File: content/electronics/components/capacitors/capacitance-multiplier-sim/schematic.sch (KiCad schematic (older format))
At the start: 7 parts, among them Q1 2N2222

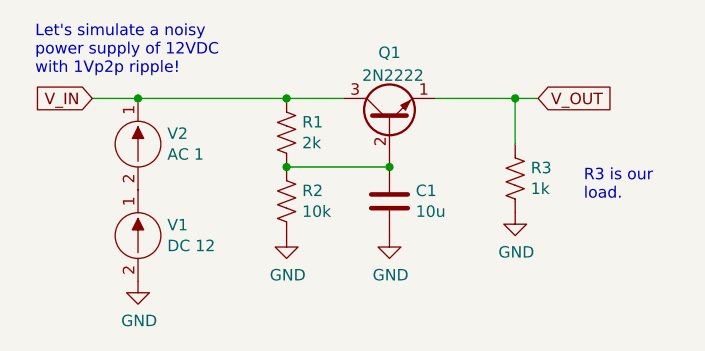
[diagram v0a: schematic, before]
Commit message: Updated the capacitance multiplier worked example.
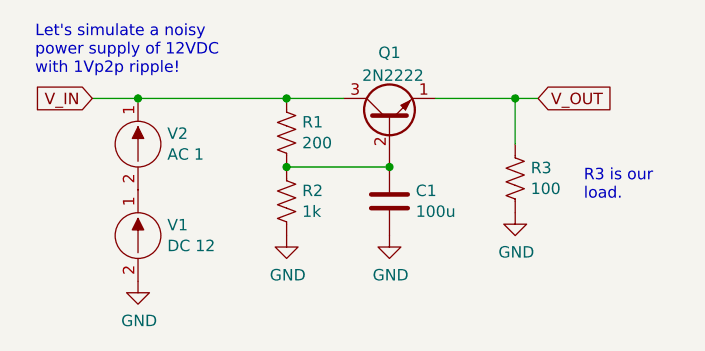
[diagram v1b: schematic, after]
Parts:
- C1: value 10u -> 100u
- R1: value 2k -> 200
- R2: value 10k -> 1k
- R3: value 1k -> 100
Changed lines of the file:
@@
 P 4500 3650
 F 0 "C1" H 4615 3696 50  0000 L CNN
-F 1 "10u" H 4615 3605 50  0000 L CNN
+F 1 "100u" H 4615 3605 50  0000 L CNN
 F 2 "" H 4700 2850 50  0001 L CNN
 F 3 "" H 4500 3650 50  0001 L CNN
@@
 P 4050 3350
 F 0 "R1" H 3982 3304 50  0000 R CNN
-F 1 "2k" H 3982 3395 50  0000 R CNN
+F 1 "200" H 3982 3395 50  0000 R CNN
 F 2 "" H 4150 2650 50  0001 L CNN
 F 3 "" H 4050 3350 50  0001 L CNN
@@
 P 4050 3650
 F 0 "R2" H 3982 3604 50  0000 R CNN
-F 1 "10k" H 3982 3695 50  0000 R CNN
+F 1 "1k" H 3982 3695 50  0000 R CNN
 F 2 "" H 4150 2950 50  0001 L CNN
 F 3 "" H 4050 3650 50  0001 L CNN
@@
 P 5050 3550
 F 0 "R3" H 4982 3504 50  0000 R CNN
-F 1 "1k" H 4982 3595 50  0000 R CNN
+F 1 "100" H 4982 3595 50  0000 R CNN
 F 2 "" H 5150 2850 50  0001 L CNN
 F 3 "" H 5050 3550 50  0001 L CNN
